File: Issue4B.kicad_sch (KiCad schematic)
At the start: 214 parts, among them IC1 ULA, IC10 4116, IC11 4116, IC12 4116, IC13 4116, IC14 LM1889, IC15 4532, IC16 4532, IC17 4532, IC18 4532, IC19 4532, IC2 Z80, IC20 4532, IC21 4532, IC22 4532, IC23 LS32, IC24 LS00, IC25 LS157, IC26 LS157, IC3 LS157, IC4 LS157, IC5 ROM, IC6 4116, IC7 4116, IC8 4116, IC9 4116, J7 Barrel_Jack_MountingPin, SW1 SW_SPDT, T1 Transformer_1P_1S, X1 14Mhz, X2 4.43Mhz

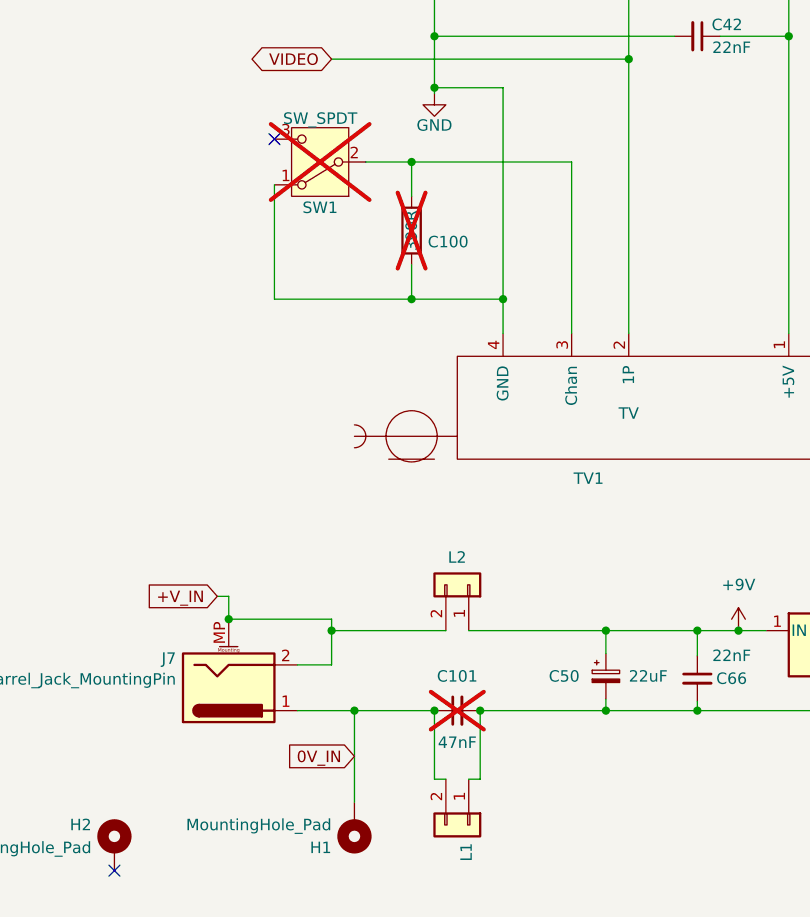
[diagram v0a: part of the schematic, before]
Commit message: Correct values for C100 and C101
Update values and layout for C100 and C101. Taken from Issue 6A schematic.
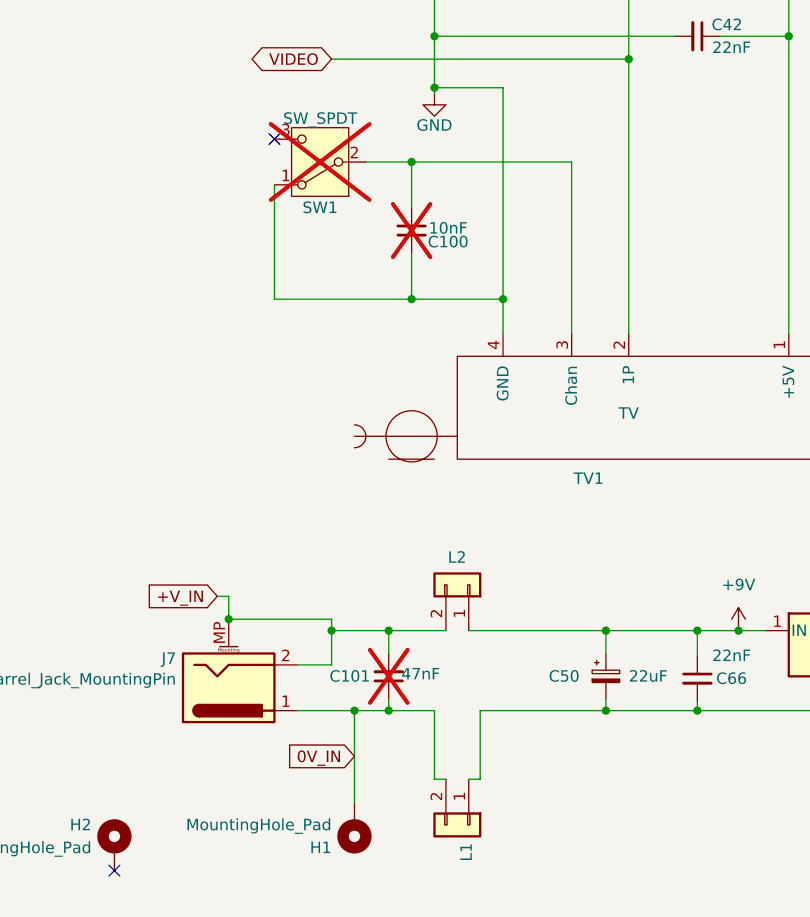
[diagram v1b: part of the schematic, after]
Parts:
- C100: value 390R -> 10nF; footprint Mod:R_Yageo_L3.6mm_D1.6mm_P12.70mm_Horizontal -> Mod:C_Axial_L3.8mm_D2.6mm_P12.70mm_Horizontal; symbol Device:R -> Device:C_Small
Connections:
- net +V_IN: now also C101.2
- net GND: no longer C101.2
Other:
- company: Submeson Brain Corporation -> Submeson Brain Corporation/LiveBoxAndy/Dee
- moved on the sheet: C101
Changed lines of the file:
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@@
 	(title_block
 		(title "ZX Spectrum 48K")
-		(date "2026-10-01")
+		(date "2026-10-08")
 		(rev "4B")
-		(company "Submeson Brain Corporation")
+		(company "Submeson Brain Corporation/LiveBoxAndy/Dee")
 	)
 	(text "X1 14Mhz\nX2 4.433619Mhz +/- 10PPM ABSOLUTE\nALL DIODES UNLESS STATED ARE 1N4148\n\nALTERNATE VALUES GIVEN FOR R56, R63, R49 & R47 ARE USED IF THE ULA\nFITTED IS OF TYPE 6C0001\n\nC61 DELETED ON ISSUE 4B\nON MOST ISSUE 4A BOARDS DCDC CONVERTER MOD NOT IMPLEMENTED."
@@
 	)
 	(junction
+		(at 77.47 351.79)
+		(diameter 0)
+		(color 0 0 0 0)
+	)
+	(junction
 		(at 233.68 80.01)
 		(diameter 0)
@@
 	)
 	(junction
+		(at 77.47 360.68)
+		(diameter 0)
+		(color 0 0 0 0)
+	)
+	(junction
 		(at 327.66 334.01)
 		(diameter 0)
@@
 	)
 	(junction
-		(at 87.63 360.68)
-		(diameter 0)
-		(color 0 0 0 0)
-	)
-	(junction
 		(at 184.15 140.97)
 		(diameter 0)
@@
 	)
 	(junction
-		(at 82.55 360.68)
-		(diameter 0)
-		(color 0 0 0 0)
-	)
-	(junction
 		(at 642.874 472.44)
 		(diameter 0)
@@
 	(wire
 		(pts
+			(xy 77.47 354.33) (xy 77.47 351.79)
+		)
+		(stroke
+			(width 0)
+			(type default)
+		)
+	)
+	(wire
+		(pts
 			(xy 627.38 186.69) (xy 627.38 125.73)
 		)
@@
 	(wire
 		(pts
+			(xy 77.47 359.41) (xy 77.47 360.68)
+		)
+		(stroke
+			(width 0)
+			(type default)
+		)
+	)
+	(wire
+		(pts
 			(xy 440.69 219.71) (xy 492.76 219.71)
 		)
@@
 	(wire
 		(pts
-			(xy 80.01 299.72) (xy 80.01 303.53)
+			(xy 80.01 299.72) (xy 80.01 304.8)
 		)
 		(stroke
@@
 	(wire
 		(pts
+			(xy 77.47 360.68) (xy 73.66 360.68)
+		)
+		(stroke
+			(width 0)
+			(type default)
+		)
+	)
+	(wire
+		(pts
 			(xy 287.02 372.872) (xy 287.02 382.27)
 		)
@@
 	(wire
 		(pts
-			(xy 80.01 311.15) (xy 80.01 314.96)
+			(xy 80.01 309.88) (xy 80.01 314.96)
 		)
 		(stroke
@@
 	(wire
 		(pts
-			(xy 82.55 360.68) (xy 73.66 360.68)
+			(xy 82.55 360.68) (xy 77.47 360.68)
 		)
 		(stroke
@@
 	(wire
 		(pts
+			(xy 77.47 351.79) (xy 83.82 351.79)
+		)
+		(stroke
+			(width 0)
+			(type default)
+		)
+	)
+	(wire
+		(pts
 			(xy 328.93 161.29) (xy 334.01 161.29)
 		)
@@
 	(wire
 		(pts
-			(xy 71.12 351.79) (xy 83.82 351.79)
+			(xy 71.12 351.79) (xy 77.47 351.79)
 		)
 		(stroke
@@
 	)
 	(symbol
-		(lib_id "Device:R")
+		(lib_name "C_Small_1")
+		(lib_id "Device:C_Small")
 		(at 80.01 307.34 0)
 		(unit 1)
@@
 			)
 		)
-		(property "Value" "390R"
-			(at 80.01 307.34 90)
+		(property "Value" "10nF"
+			(at 84.074 307.086 0)
 			(show_name no)
 			(do_not_autoplace no)
@@
 			)
 		)
-		(property "Footprint" "Mod:R_Yageo_L3.6mm_D1.6mm_P12.70mm_Horizontal"
-			(at 78.232 307.34 90)
+		(property "Footprint" "Mod:C_Axial_L3.8mm_D2.6mm_P12.70mm_Horizontal"
+			(at 80.01 307.34 0)
 			(hide yes)
 			(show_name no)
@@
 			)
 		)
-		(property "Description" ""
-			(at 80.01 307.34 0)
+		(property "Description" "Unpolarized capacitor, small symbol"
+			(at 80.01 317.5 0)
+			(hide yes)
 			(show_name no)
 			(do_not_autoplace no)
@@
 	(symbol
 		(lib_id "Device:C_Small")
-		(at 85.09 360.68 90)
+		(at 77.47 356.87 0)
 		(mirror x)
 		(unit 1)
@@
 		(dnp yes)
 		(property "Reference" "C101"
-			(at 85.09 356.87 90)
+			(at 73.152 356.87 0)
 			(show_name no)
 			(do_not_autoplace no)
@@
 		)
 		(property "Value" "47nF"
-			(at 85.09 364.236 90)
+			(at 81.026 356.616 0)
 			(show_name no)
 			(do_not_autoplace no)
@@
 		)
 		(property "Footprint" "Mod:C_Axial_L3.8mm_D2.6mm_P12.70mm_Horizontal"
-			(at 85.09 360.68 0)
+			(at 77.47 356.87 0)
 			(hide yes)
 			(show_name no)
@@
 		)
 		(property "Datasheet" "https://www.vishay.com/doc?45164"
-			(at 85.09 360.68 0)
+			(at 77.47 356.87 0)
 			(hide yes)
 			(show_name no)
@@
 		)
 		(property "Description" "Capacitor Ceramic MLCC"
-			(at 85.09 360.68 0)
+			(at 77.47 356.87 0)
 			(hide yes)
 			(show_name no)
